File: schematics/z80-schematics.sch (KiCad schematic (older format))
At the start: 46 parts, among them P1 FTDI SERIAL, SW1 SW_PUSH, SW2 SW_PUSH, U1 Z80-CPU, U10 Z80-CTC, U11 Z80-SIO/0, U12 74HC574, U13 74HC541, U2 AS6C1008, U3 CAT28C256BL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

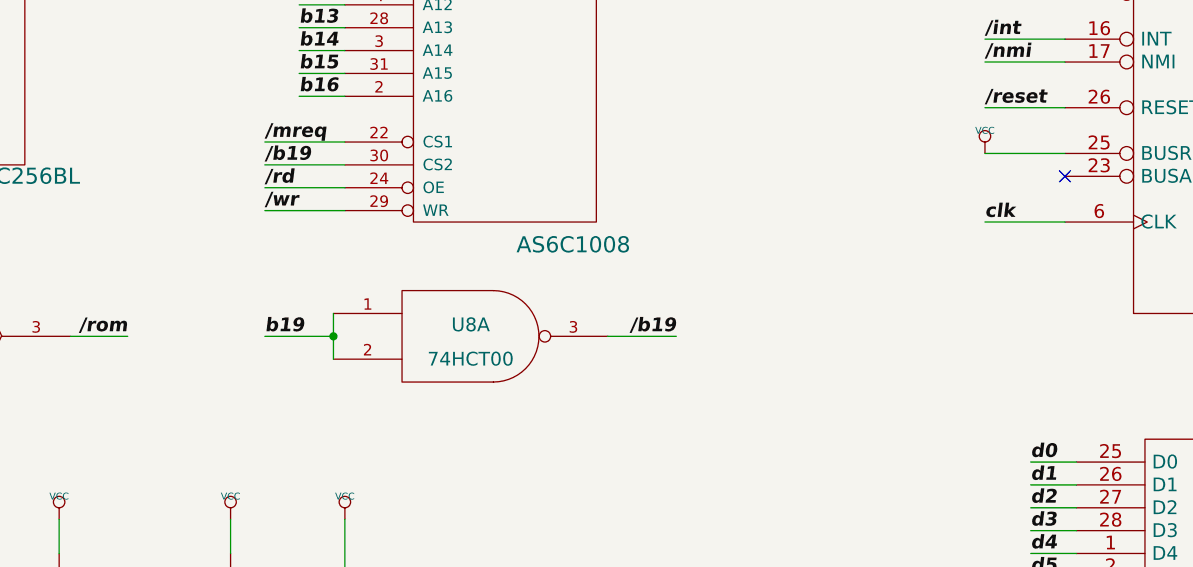
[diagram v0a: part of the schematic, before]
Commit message: Add support for read-only RAM mapping
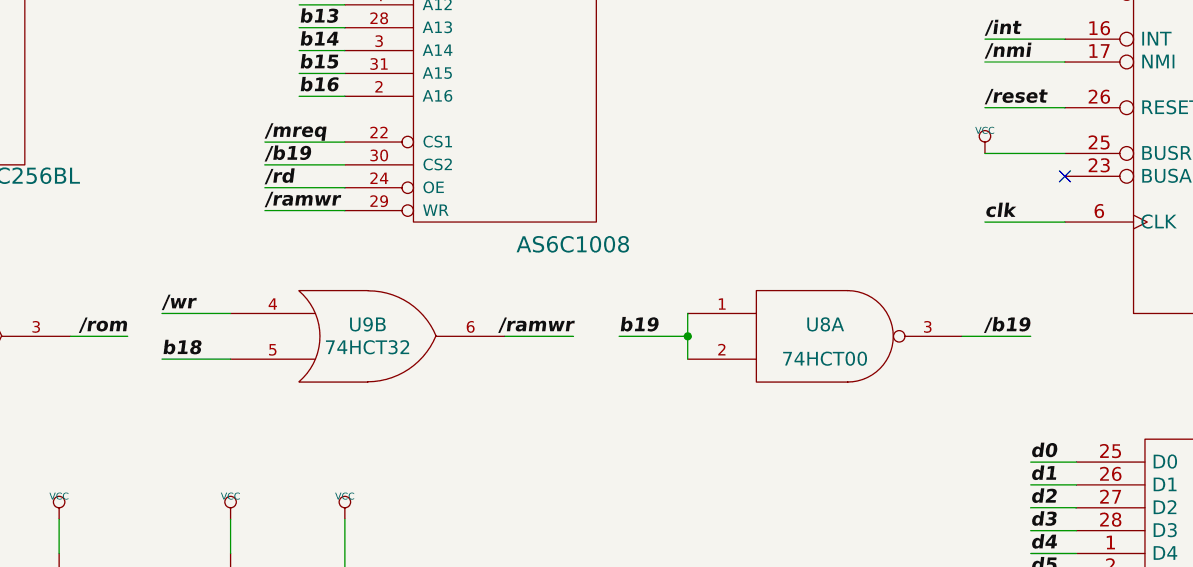
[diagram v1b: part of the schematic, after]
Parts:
- added unit 2 of U9
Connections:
- net +5V: now also U9.14 (VCC)
- net /wr: now also U9.4; no longer U2.29 (WR)
- net GND: now also U9.7 (GND)
- net b18: now also U9.5
- new net /ramwr: U2.29 (WR), U9.6
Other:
- moved on the sheet: U8A
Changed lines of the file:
@@
 L 7400 U8
 U 1 1 54376642
-P 4050 3450
-F 0 "U8" H 4050 3500 60  0000 C CNN
-F 1 "74HCT00" H 4050 3350 60  0000 C CNN
-F 2 "~" H 4050 3450 60  0000 C CNN
-F 3 "~" H 4050 3450 60  0000 C CNN
-	1    4050 3450
-	1    0    0    -1
-$EndComp
-Text Label 3150 3450 0    60   Italic 12
+P 5600 3450
+F 0 "U8" H 5600 3500 60  0000 C CNN
+F 1 "74HCT00" H 5600 3350 60  0000 C CNN
+F 2 "~" H 5600 3450 60  0000 C CNN
+F 3 "~" H 5600 3450 60  0000 C CNN
+	1    5600 3450
+	1    0    0    -1
+$EndComp
+Text Label 4700 3450 0    60   Italic 12
 b19
 Text Label 11200 1750 2    60   Italic 12
@@
 /reset
 Text Label 3150 2900 0    60   Italic 12
-/wr
+/ramwr
 Text Label 800  2550 0    60   Italic 12
 /rd
@@
 Text Label 2550 3450 2    60   Italic 12
 /rom
-Text Label 4950 3450 2    60   Italic 12
+Text Label 6500 3450 2    60   Italic 12
 /b19
 Text Label 3150 2700 0    60   Italic 12
@@
 	800  3550 1100 3550
 Wire Wire Line
-	3450 3350 3450 3550
-Wire Wire Line
-	3450 3450 3150 3450
-Connection ~ 3450 3450
-Wire Wire Line
-	4650 3450 4950 3450
+	5000 3350 5000 3550
+Wire Wire Line
+	5000 3450 4700 3450
+Connection ~ 5000 3450
+Wire Wire Line
+	6200 3450 6500 3450
 Wire Wire Line
 	1100 3350 800  3350
@@
 Connection ~ 3500 7000
 $Comp
-L VCC #PWR?
+L VCC #PWR029
 U 1 1 5725E77F
 P 6700 7800
-F 0 "#PWR?" H 6700 7650 50  0001 C CNN
+F 0 "#PWR029" H 6700 7650 50  0001 C CNN
 F 1 "VCC" H 6700 7950 50  0000 C CNN
 F 2 "" H 6700 7800 50  0000 C CNN
@@
 NoConn ~ 6900 7700
 $Comp
-L VCC #PWR?
+L VCC #PWR030
 U 1 1 5725EC6B
 P 6700 9100
-F 0 "#PWR?" H 6700 8950 50  0001 C CNN
+F 0 "#PWR030" H 6700 8950 50  0001 C CNN
 F 1 "VCC" H 6700 9250 50  0000 C CNN
 F 2 "" H 6700 9100 50  0000 C CNN
@@
 	6700 9100 6900 9100
 NoConn ~ 6900 9200
+$Comp
+L 74LS32 U9
+U 2 1 572614F7
+P 3600 3450
+F 0 "U9" H 3600 3500 60  0000 C CNN
+F 1 "74HCT32" H 3600 3400 60  0000 C CNN
+F 2 "~" H 3600 3450 60  0000 C CNN
+F 3 "~" H 3600 3450 60  0000 C CNN
+	2    3600 3450
+	1    0    0    -1
+$EndComp
+Wire Wire Line
+	4200 3450 4500 3450
+Text Label 4500 3450 2    60   Italic 12
+/ramwr
+Wire Wire Line
+	3000 3350 2700 3350
+Text Label 2700 3350 0    60   Italic 12
+/wr
+Wire Wire Line
+	3000 3550 2700 3550
+Text Label 2700 3550 0    60   Italic 12
+b18
 $EndSCHEMATC

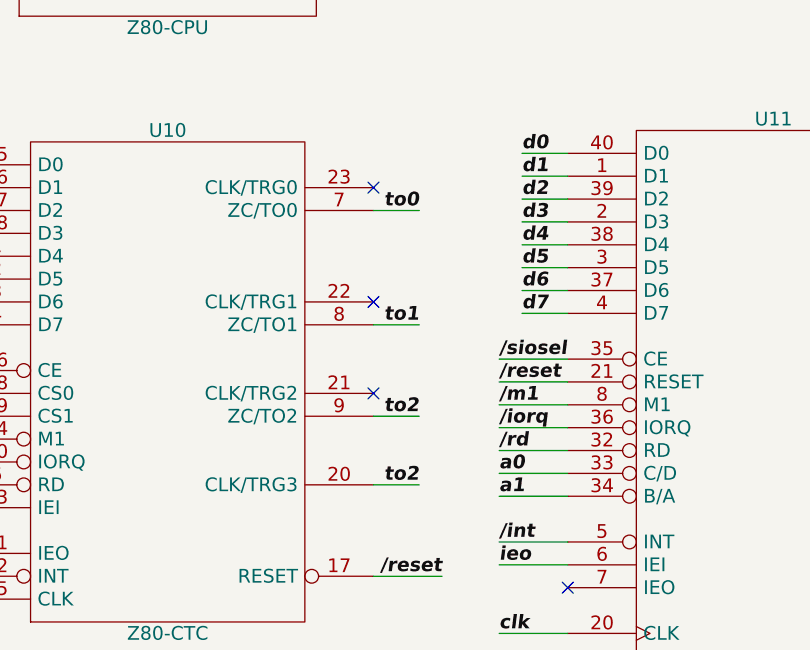
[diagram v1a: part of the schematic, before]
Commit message: Enable use of CTC counter mode, to avoid pre-scale on serial clock
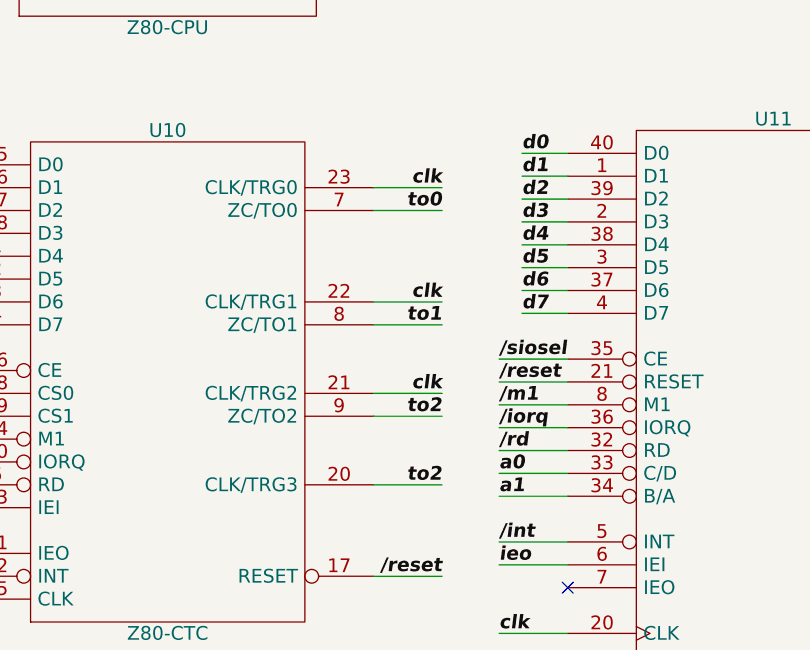
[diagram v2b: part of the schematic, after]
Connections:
- net clk: now also U10.21 (CLK/TRG2), U10.22 (CLK/TRG1), U10.23 (CLK/TRG0)
- no-connect marks 42 -> 39
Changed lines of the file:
@@
 Text Label 6300 5400 0    60   Italic 12
 /rd
-Text Label 8700 4200 2    60   Italic 12
+Text Label 8800 4200 2    60   Italic 12
 to0
 Text Label 11350 4050 2    60   Italic 12
 to0
-Text Label 8700 4700 2    60   Italic 12
+Text Label 8800 4700 2    60   Italic 12
 to1
 Text Label 11350 5350 2    60   Italic 12
@@
 Text Label 9050 5150 0    60   Italic 12
 /iorq
-Text Label 8700 5100 2    60   Italic 12
+Text Label 8800 5100 2    60   Italic 12
 to2
-Text Label 8700 5400 2    60   Italic 12
+Text Label 8800 5400 2    60   Italic 12
 to2
 Text Label 6400 5700 0    60   Italic 12
@@
 Text Label 9050 5450 0    60   Italic 12
 a1
-NoConn ~ 8500 5000
-NoConn ~ 8500 4600
-NoConn ~ 8500 4100
 $Comp
 L CONN_6 P1
@@
 	6700 5400 6300 5400
 Wire Wire Line
-	8500 4200 8700 4200
-Wire Wire Line
 	11150 4050 11350 4050
 Wire Wire Line
-	8500 4700 8700 4700
-Wire Wire Line
 	11150 5350 11350 5350
 Wire Wire Line
@@
 Wire Wire Line
 	9350 5150 9050 5150
-Wire Wire Line
-	8500 5100 8700 5100
-Wire Wire Line
-	8500 5400 8700 5400
 Wire Wire Line
 	6700 5700 6400 5700
@@
 Text Label 2700 3550 0    60   Italic 12
 b18
+Wire Wire Line
+	8500 4200 8800 4200
+Wire Wire Line
+	8500 4700 8800 4700
+Wire Wire Line
+	8500 5100 8800 5100
+Wire Wire Line
+	8500 5400 8800 5400
+Wire Wire Line
+	8500 4100 8800 4100
+Wire Wire Line
+	8500 4600 8800 4600
+Wire Wire Line
+	8500 5000 8800 5000
+Text Label 8800 4100 2    60   Italic 12
+clk
+Text Label 8800 4600 2    60   Italic 12
+clk
+Text Label 8800 5000 2    60   Italic 12
+clk
 $EndSCHEMATC
